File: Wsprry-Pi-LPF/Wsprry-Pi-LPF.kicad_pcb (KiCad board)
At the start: 2 copper layers, 36.8 x 12.4 mm, 13 parts, among them J1 Conn_01x04, J2 Conn_01x04

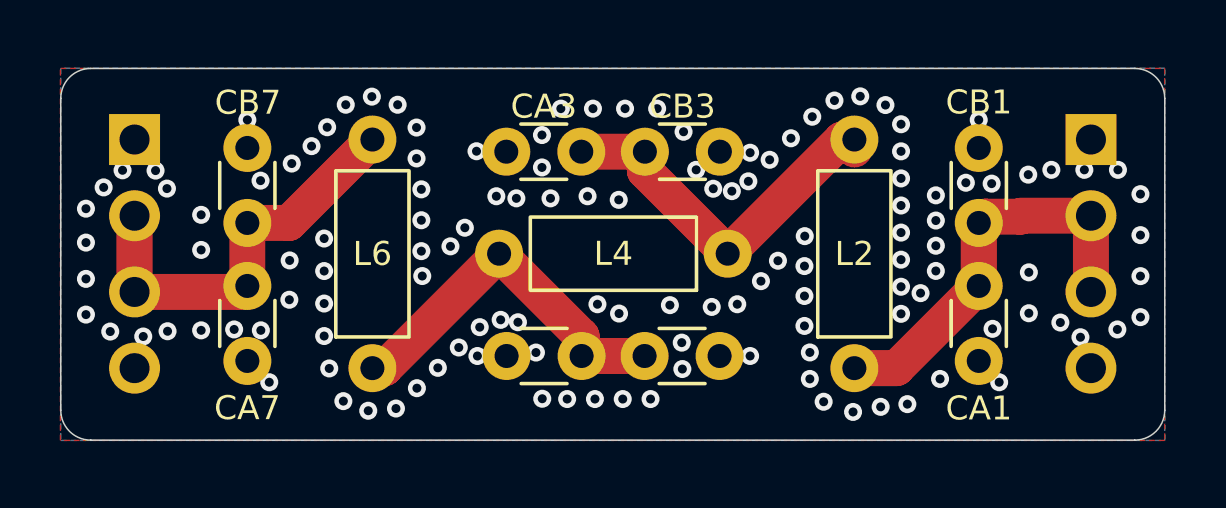
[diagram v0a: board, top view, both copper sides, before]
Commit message: Enlarge axial L pad, add Toroid co-pad
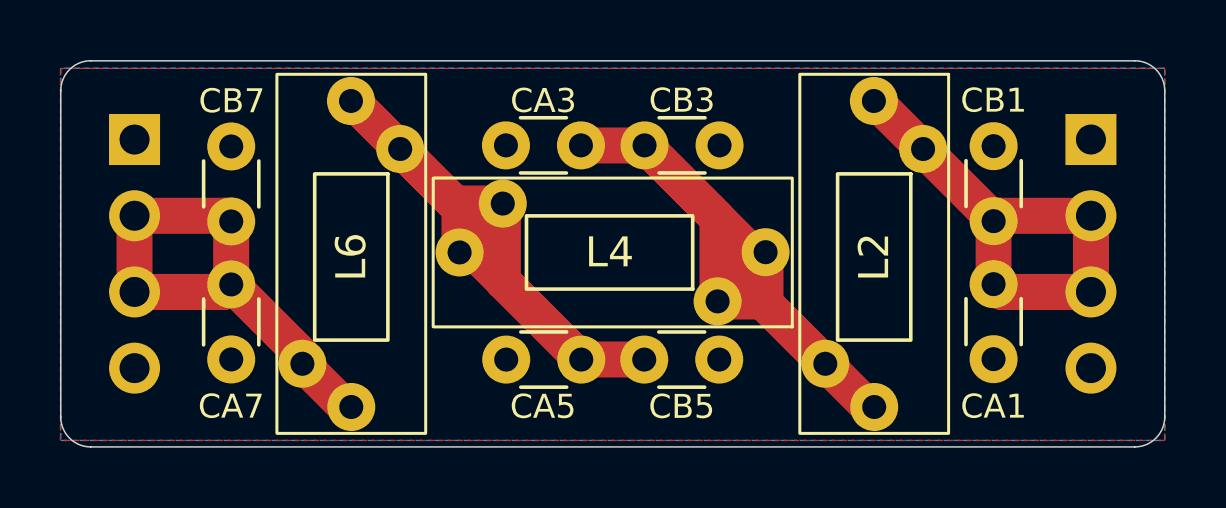
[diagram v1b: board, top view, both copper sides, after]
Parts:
- L2, L4, L6: footprint Inductor_THT:L_Axial_L5.3mm_D2.2mm_P7.62mm_Horizontal_Vishay_IM-1 -> Wsprry Pi LPF:L_Axial_Horiz_Torroid_Vert_12mm_D5mm_P10.2mm
- moved L4 3.94 mm to (136.9, 99.1)
- moved L6 3.77 mm to (128.3, 99.2), turned to -90 degrees
- moved L2 3.76 mm to (145.7, 99.2), turned to -90 degrees
- moved CA7 0.54 mm to (124.3, 102.6)
- moved CB7 0.54 mm to (124.3, 95.5)
- moved CA1 0.50 mm to (149.7, 102.6)
- moved CB1 0.50 mm to (149.7, 95.5)
- moved CA3 0.21 mm to (133.4, 95.5)
- moved CB3 0.21 mm to (140.5, 95.5)
- moved CA5 0.12 mm to (133.4, 102.6)
- moved CB5 0.12 mm to (140.5, 102.6)
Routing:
- net Net-(CA3-Pad2): track 12.8 -> 27.4 mm
- net Net-(CA5-Pad2): track 12.5 -> 26.9 mm
- net /RF_OUT: track 13.8 -> 17.1 mm
- net /RF_IN: track 13.8 -> 17.0 mm
- net GND: vias 132 -> 0
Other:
- board size 36.8 x 12.4 mm -> 36.8 x 12.9 mm
- board text added: "Lee Bussy [AA0NT]"
- board text added: "Wsprry Pi LPF v1.0.1"
- board text removed: "Wsprry Pi LPF v1.0.0 Lee Bussy [AA0NT]"
